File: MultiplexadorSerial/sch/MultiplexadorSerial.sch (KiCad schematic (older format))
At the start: 57 parts, among them Q1 Q_NPN_CBE, Q2 Q_NPN_CBE, Q3 Q_NPN_CBE, Q4 Q_NPN_CBE, U1 SP3481CP, U2 SP3481CP, U3 SP3481CP, U4 SP3481CP, U5 4052

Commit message: Posicionamento MultiplexadorSerial Signed-off-by: cuki2 <mauricio@krebs.com.br>
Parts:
- removed Q1, Q2, Q4: Q_NPN_CBE, symbol Q_NPN_CBE
- added Q1, Q2, Q4: Q_NPN_CBE, w_to:to92_3, symbol Q_NPN_EBC
- D1: footprint w_indicators:led_3mm_red -> w_indicators:led_3mm_green
- Q3: footprint (none) -> w_to:to92_3; symbol Q_NPN_CBE -> Q_NPN_EBC
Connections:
- net GND: now also Q3.1 (E), Q1.1 (E), Q2.1 (E), Q4.1 (E); no longer Q3.3 (E)
- net at R21.2, U3.2 (~RE~), U3.3 (DE): now also Q3.3 (C); no longer Q3.1 (C)
- net at R22.2, U4.2 (~RE~), U4.3 (DE): now also Q4.3 (C)
- net at R18.1: now also Q4.2 (B)
- net at R5.2, U1.2 (~RE~), U1.3 (DE): now also Q1.3 (C)
- net at R1.1: now also Q1.2 (B)
- net at R6.2, U2.2 (~RE~), U2.3 (DE): now also Q2.3 (C)
- net at R2.1: now also Q2.2 (B)
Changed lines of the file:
@@
 $EndComp
 $Comp
-L GND #PWR01
+L GND #PWR21
 U 1 1 59F1E27D
 P 9850 2750
-F 0 "#PWR01" H 9850 2500 50  0001 C CNN
+F 0 "#PWR21" H 9850 2500 50  0001 C CNN
 F 1 "GND" H 9850 2600 50  0000 C CNN
 F 2 "" H 9850 2750 50  0001 C CNN
@@
 $EndComp
 $Comp
-L GND #PWR02
+L GND #PWR13
 U 1 1 59F1F03E
 P 6400 2750
-F 0 "#PWR02" H 6400 2500 50  0001 C CNN
+F 0 "#PWR13" H 6400 2500 50  0001 C CNN
 F 1 "GND" H 6400 2600 50  0000 C CNN
 F 2 "" H 6400 2750 50  0001 C CNN
@@
 $EndComp
 $Comp
-L GND #PWR03
+L GND #PWR11
 U 1 1 59F1FB71
 P 5850 3750
-F 0 "#PWR03" H 5850 3500 50  0001 C CNN
+F 0 "#PWR11" H 5850 3500 50  0001 C CNN
 F 1 "GND" H 5850 3600 50  0000 C CNN
 F 2 "" H 5850 3750 50  0001 C CNN
@@
 $EndComp
 $Comp
-L GND #PWR04
+L GND #PWR15
 U 1 1 59F20200
 P 6450 3900
-F 0 "#PWR04" H 6450 3650 50  0001 C CNN
+F 0 "#PWR15" H 6450 3650 50  0001 C CNN
 F 1 "GND" H 6450 3750 50  0000 C CNN
 F 2 "" H 6450 3900 50  0001 C CNN
@@
 $EndComp
 $Comp
-L GND #PWR05
+L GND #PWR20
 U 1 1 59F215E7
 P 9250 4550
-F 0 "#PWR05" H 9250 4300 50  0001 C CNN
+F 0 "#PWR20" H 9250 4300 50  0001 C CNN
 F 1 "GND" H 9250 4400 50  0000 C CNN
 F 2 "" H 9250 4550 50  0001 C CNN
@@
 $EndComp
 $Comp
-L Q_NPN_CBE Q3
+L Q_NPN_EBC Q3
 U 1 1 59F228FE
 P 4650 3650
 F 0 "Q3" H 4850 3700 50  0000 L CNN
 F 1 "Q_NPN_CBE" H 4850 3600 50  0000 L CNN
-F 2 "" H 4850 3750 50  0001 C CNN
+F 2 "w_to:to92_3" H 4850 3750 50  0001 C CNN
 F 3 "" H 4650 3650 50  0001 C CNN
 	1    4650 3650
@@
 $EndComp
 $Comp
-L GND #PWR06
+L GND #PWR9
 U 1 1 59F22AFE
 P 4750 3950
-F 0 "#PWR06" H 4750 3700 50  0001 C CNN
+F 0 "#PWR9" H 4750 3700 50  0001 C CNN
 F 1 "GND" H 4750 3800 50  0000 C CNN
 F 2 "" H 4750 3950 50  0001 C CNN
@@
 $EndComp
 $Comp
-L GND #PWR07
+L GND #PWR22
 U 1 1 59F26F62
 P 10100 1000
-F 0 "#PWR07" H 10100 750 50  0001 C CNN
+F 0 "#PWR22" H 10100 750 50  0001 C CNN
 F 1 "GND" H 10100 850 50  0000 C CNN
 F 2 "" H 10100 1000 50  0001 C CNN
@@
 $EndComp
 $Comp
-L GND #PWR08
+L GND #PWR18
 U 1 1 59F27359
 P 7650 1700
-F 0 "#PWR08" H 7650 1450 50  0001 C CNN
+F 0 "#PWR18" H 7650 1450 50  0001 C CNN
 F 1 "GND" H 7650 1550 50  0000 C CNN
 F 2 "" H 7650 1700 50  0001 C CNN
@@
 $EndComp
 $Comp
-L GND #PWR09
+L GND #PWR14
 U 1 1 59F28089
 P 6400 5450
-F 0 "#PWR09" H 6400 5200 50  0001 C CNN
+F 0 "#PWR14" H 6400 5200 50  0001 C CNN
 F 1 "GND" H 6400 5300 50  0000 C CNN
 F 2 "" H 6400 5450 50  0001 C CNN
@@
 $EndComp
 $Comp
-L GND #PWR010
+L GND #PWR12
 U 1 1 59F280AE
 P 5850 6450
-F 0 "#PWR010" H 5850 6200 50  0001 C CNN
+F 0 "#PWR12" H 5850 6200 50  0001 C CNN
 F 1 "GND" H 5850 6300 50  0000 C CNN
 F 2 "" H 5850 6450 50  0001 C CNN
@@
 $EndComp
 $Comp
-L GND #PWR011
+L GND #PWR16
 U 1 1 59F280BC
 P 6450 6600
-F 0 "#PWR011" H 6450 6350 50  0001 C CNN
+F 0 "#PWR16" H 6450 6350 50  0001 C CNN
 F 1 "GND" H 6450 6450 50  0000 C CNN
 F 2 "" H 6450 6600 50  0001 C CNN
@@
 $EndComp
 $Comp
-L Q_NPN_CBE Q4
-U 1 1 59F280E2
-P 4650 6350
-F 0 "Q4" H 4850 6400 50  0000 L CNN
-F 1 "Q_NPN_CBE" H 4850 6300 50  0000 L CNN
-F 2 "" H 4850 6450 50  0001 C CNN
-F 3 "" H 4650 6350 50  0001 C CNN
-	1    4650 6350
-	1    0    0    -1
-$EndComp
-$Comp
-L GND #PWR012
+L GND #PWR10
 U 1 1 59F280E9
 P 4750 6650
-F 0 "#PWR012" H 4750 6400 50  0001 C CNN
+F 0 "#PWR10" H 4750 6400 50  0001 C CNN
 F 1 "GND" H 4750 6500 50  0000 C CNN
 F 2 "" H 4750 6650 50  0001 C CNN
@@
 $EndComp
 $Comp
-L GND #PWR013
+L GND #PWR5
 U 1 1 59F2BE74
 P 2850 5650
-F 0 "#PWR013" H 2850 5400 50  0001 C CNN
+F 0 "#PWR5" H 2850 5400 50  0001 C CNN
 F 1 "GND" H 2850 5500 50  0000 C CNN
 F 2 "" H 2850 5650 50  0001 C CNN
@@
 $EndComp
 $Comp
-L GND #PWR014
+L GND #PWR3
 U 1 1 59F2BE99
 P 2300 6650
-F 0 "#PWR014" H 2300 6400 50  0001 C CNN
+F 0 "#PWR3" H 2300 6400 50  0001 C CNN
 F 1 "GND" H 2300 6500 50  0000 C CNN
 F 2 "" H 2300 6650 50  0001 C CNN
@@
 $EndComp
 $Comp
-L GND #PWR015
+L GND #PWR6
 U 1 1 59F2BEA7
 P 2900 6800
-F 0 "#PWR015" H 2900 6550 50  0001 C CNN
+F 0 "#PWR6" H 2900 6550 50  0001 C CNN
 F 1 "GND" H 2900 6650 50  0000 C CNN
 F 2 "" H 2900 6800 50  0001 C CNN
@@
 $EndComp
 $Comp
-L Q_NPN_CBE Q1
-U 1 1 59F2BECC
-P 1100 6550
-F 0 "Q1" H 1300 6600 50  0000 L CNN
-F 1 "Q_NPN_CBE" H 1300 6500 50  0000 L CNN
-F 2 "" H 1300 6650 50  0001 C CNN
-F 3 "" H 1100 6550 50  0001 C CNN
-	1    1100 6550
-	1    0    0    -1
-$EndComp
-$Comp
-L GND #PWR016
+L GND #PWR1
 U 1 1 59F2BED3
 P 1200 6850
-F 0 "#PWR016" H 1200 6600 50  0001 C CNN
+F 0 "#PWR1" H 1200 6600 50  0001 C CNN
 F 1 "GND" H 1200 6700 50  0000 C CNN
 F 2 "" H 1200 6850 50  0001 C CNN
@@
 $EndComp
 $Comp
-L GND #PWR017
+L GND #PWR7
 U 1 1 59F2EBAF
 P 2950 2400
-F 0 "#PWR017" H 2950 2150 50  0001 C CNN
+F 0 "#PWR7" H 2950 2150 50  0001 C CNN
 F 1 "GND" H 2950 2250 50  0000 C CNN
 F 2 "" H 2950 2400 50  0001 C CNN
@@
 $EndComp
 $Comp
-L GND #PWR018
+L GND #PWR4
 U 1 1 59F2EBD4
 P 2400 3400
-F 0 "#PWR018" H 2400 3150 50  0001 C CNN
+F 0 "#PWR4" H 2400 3150 50  0001 C CNN
 F 1 "GND" H 2400 3250 50  0000 C CNN
 F 2 "" H 2400 3400 50  0001 C CNN
@@
 $EndComp
 $Comp
-L GND #PWR019
+L GND #PWR8
 U 1 1 59F2EBE2
 P 3000 3550
-F 0 "#PWR019" H 3000 3300 50  0001 C CNN
+F 0 "#PWR8" H 3000 3300 50  0001 C CNN
 F 1 "GND" H 3000 3400 50  0000 C CNN
 F 2 "" H 3000 3550 50  0001 C CNN
@@
 $EndComp
 $Comp
-L Q_NPN_CBE Q2
-U 1 1 59F2EC07
-P 1200 3300
-F 0 "Q2" H 1400 3350 50  0000 L CNN
-F 1 "Q_NPN_CBE" H 1400 3250 50  0000 L CNN
-F 2 "" H 1400 3400 50  0001 C CNN
-F 3 "" H 1200 3300 50  0001 C CNN
-	1    1200 3300
-	1    0    0    -1
-$EndComp
-$Comp
-L GND #PWR020
+L GND #PWR2
 U 1 1 59F2EC0E
 P 1300 3600
-F 0 "#PWR020" H 1300 3350 50  0001 C CNN
+F 0 "#PWR2" H 1300 3350 50  0001 C CNN
 F 1 "GND" H 1300 3450 50  0000 C CNN
 F 2 "" H 1300 3600 50  0001 C CNN
@@
 F 0 "D1" H 7050 1250 50  0000 C CNN
 F 1 "PWR" H 7050 1050 50  0000 C CNN
-F 2 "w_indicators:led_3mm_red" H 7050 1150 50  0001 C CNN
+F 2 "w_indicators:led_3mm_green" H 7050 1150 50  0001 C CNN
 F 3 "" H 7050 1150 50  0001 C CNN
 	1    7050 1150
@@
 $EndComp
 $Comp
-L GND #PWR021
+L GND #PWR17
 U 1 1 59F4549D
 P 6550 1050
-F 0 "#PWR021" H 6550 800 50  0001 C CNN
+F 0 "#PWR17" H 6550 800 50  0001 C CNN
 F 1 "GND" H 6550 900 50  0000 C CNN
 F 2 "" H 6550 1050 50  0001 C CNN
@@
 	6550 900  6600 900
 $Comp
-L GND #PWR022
+L GND #PWR19
 U 1 1 59F4914C
 P 7950 4250
-F 0 "#PWR022" H 7950 4000 50  0001 C CNN
+F 0 "#PWR19" H 7950 4000 50  0001 C CNN
 F 1 "GND" H 7950 4100 50  0000 C CNN
 F 2 "" H 7950 4250 50  0001 C CNN
@@
 Wire Wire Line
 	7950 3850 8100 3850
+$Comp
+L Q_NPN_EBC Q4
+U 1 1 59F58E6E
+P 4650 6350
+F 0 "Q4" H 4850 6400 50  0000 L CNN
+F 1 "Q_NPN_CBE" H 4850 6300 50  0000 L CNN
+F 2 "w_to:to92_3" H 4850 6450 50  0001 C CNN
+F 3 "" H 4650 6350 50  0001 C CNN
+	1    4650 6350
+	1    0    0    -1
+$EndComp
+$Comp
+L Q_NPN_EBC Q1
+U 1 1 59F58F65
+P 1100 6550
+F 0 "Q1" H 1300 6600 50  0000 L CNN
+F 1 "Q_NPN_CBE" H 1300 6500 50  0000 L CNN
+F 2 "w_to:to92_3" H 1300 6650 50  0001 C CNN
+F 3 "" H 1100 6550 50  0001 C CNN
+	1    1100 6550
+	1    0    0    -1
+$EndComp
+$Comp
+L Q_NPN_EBC Q2
+U 1 1 59F59073
+P 1200 3300
+F 0 "Q2" H 1400 3350 50  0000 L CNN
+F 1 "Q_NPN_CBE" H 1400 3250 50  0000 L CNN
+F 2 "w_to:to92_3" H 1400 3400 50  0001 C CNN
+F 3 "" H 1200 3300 50  0001 C CNN
+	1    1200 3300
+	1    0    0    -1
+$EndComp
 $EndSCHEMATC

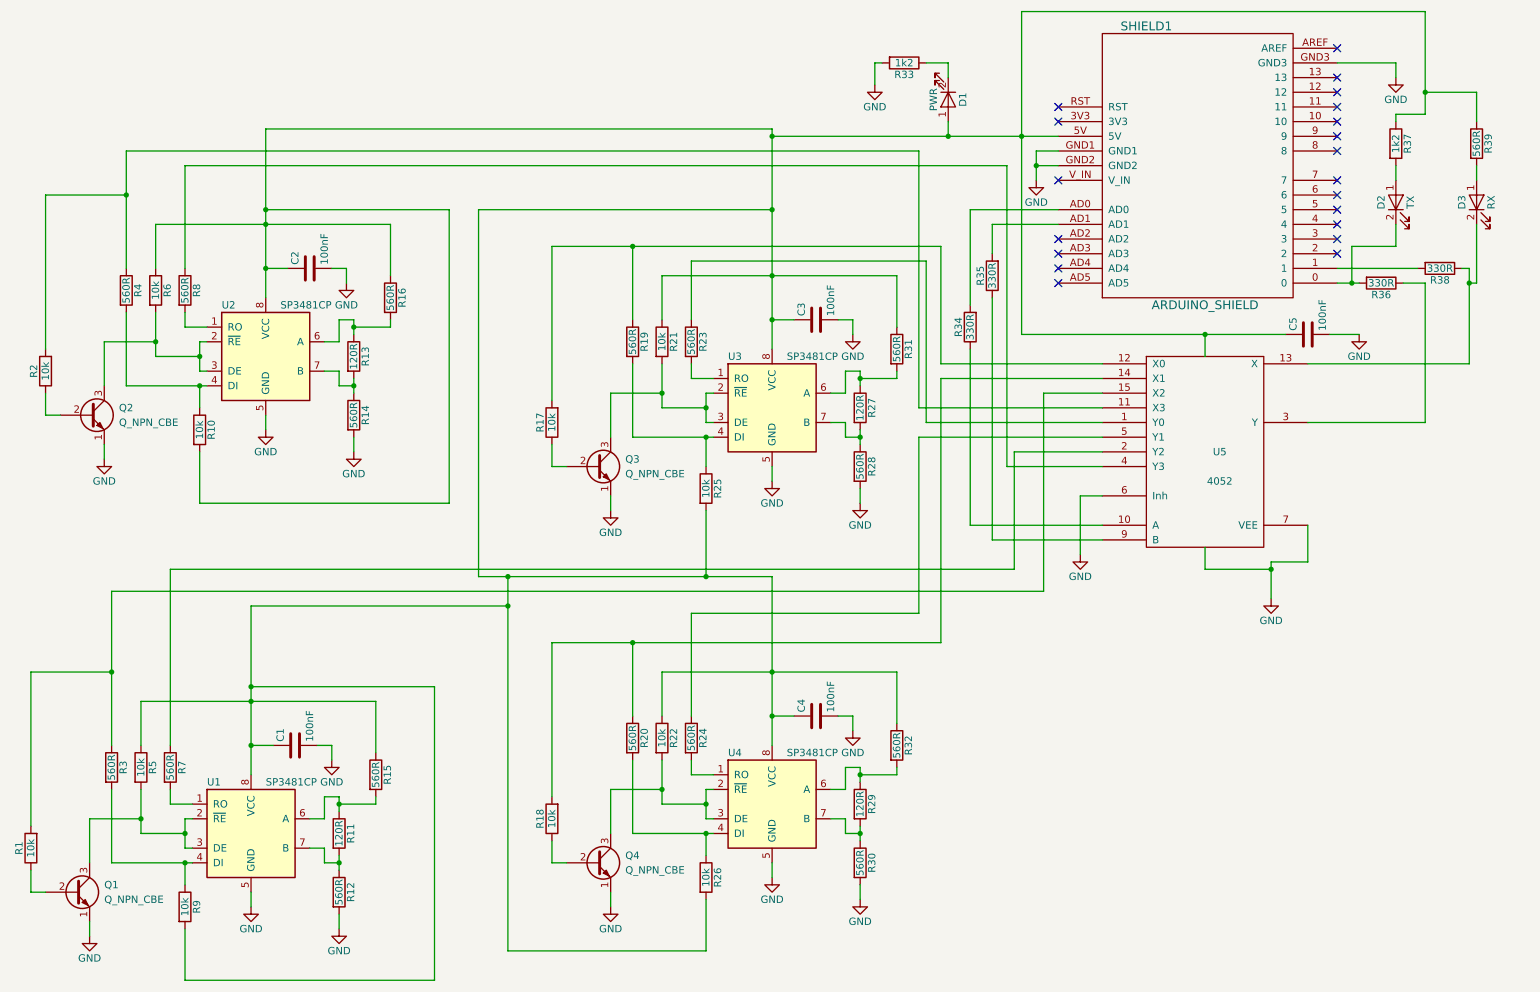
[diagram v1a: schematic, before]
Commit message: Multiplexador Serial RS485 arduino
Signed-off-by: cuki2 <mauricio@krebs.com.br>
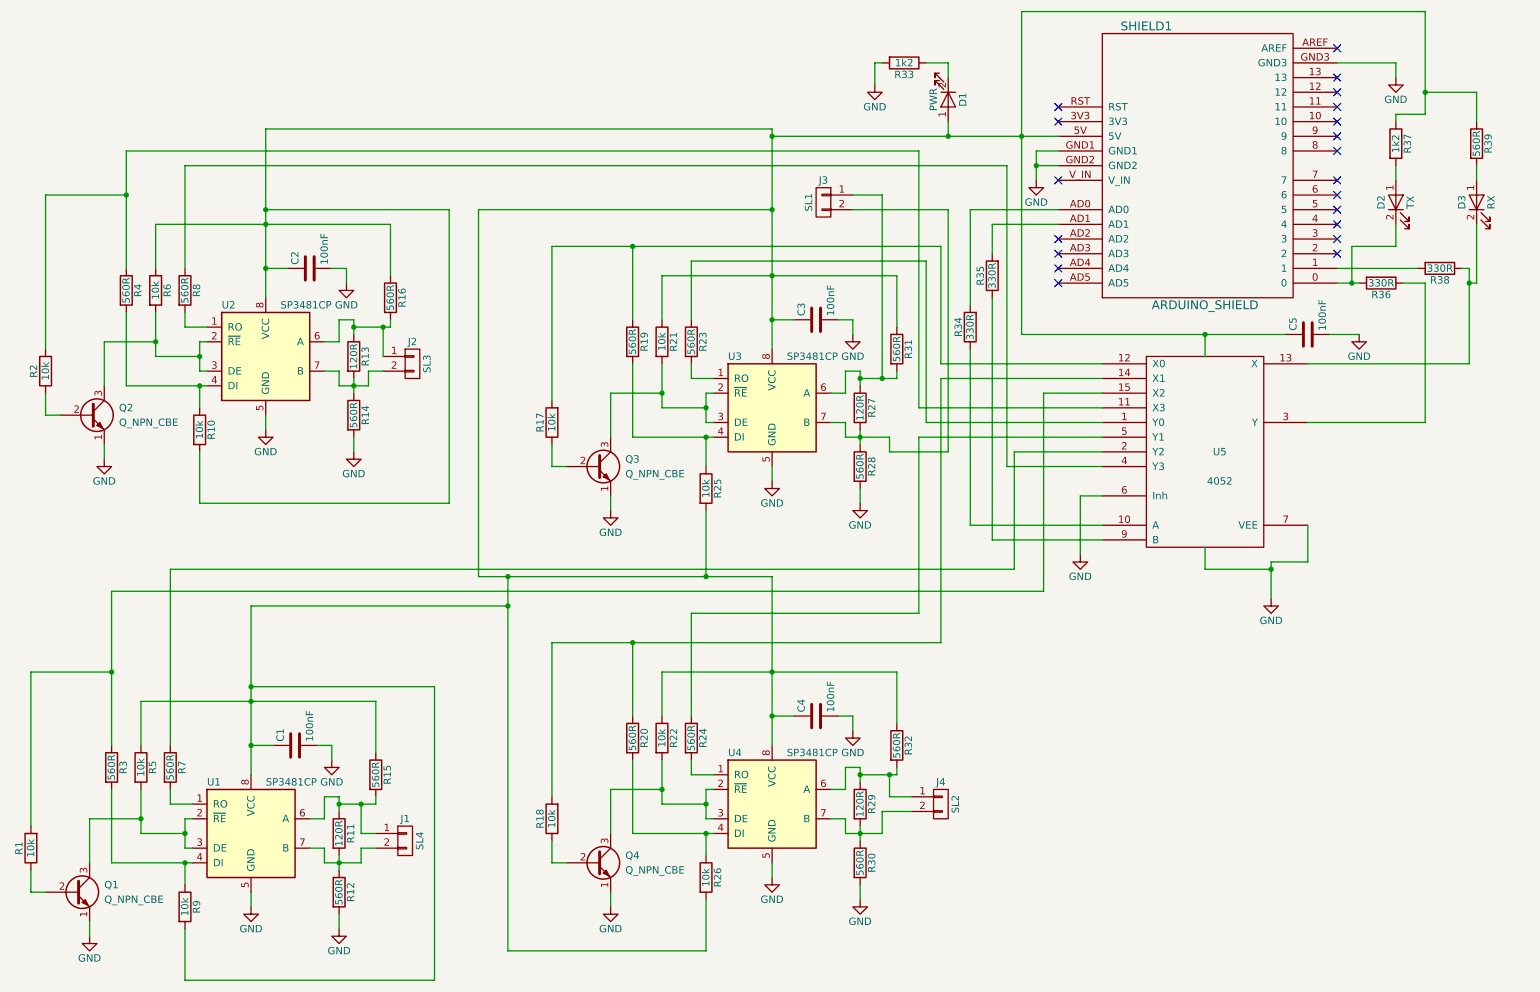
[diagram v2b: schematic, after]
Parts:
- added J1: SL4, w_pin_strip:pin_socket_2, symbol CONN_01X02
- added J2: SL3, w_pin_strip:pin_socket_2, symbol CONN_01X02
- added J3: SL1, w_pin_strip:pin_socket_2, symbol CONN_01X02
- added J4: SL2, w_pin_strip:pin_socket_2, symbol CONN_01X02
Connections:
- net at R27.1, R31.2, U3.6 (A): now also J3.1 (P1)
- net at R27.2, R28.1, U3.7 (B): now also J3.2 (P2)
- net at R29.1, R32.2, U4.6 (A): now also J4.1 (P1)
- net at R29.2, R30.1, U4.7 (B): now also J4.2 (P2)
- net at R11.1, R15.2, U1.6 (A): now also J1.1 (P1)
- net at R11.2, R12.1, U1.7 (B): now also J1.2 (P2)
- net at R13.1, R16.2, U2.6 (A): now also J2.1 (P1)
- net at R13.2, R14.1, U2.7 (B): now also J2.2 (P2)

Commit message: adicionado resistores pull ups nos transdutores
Signed-off-by: cuki2 <mauricio@krebs.com.br>
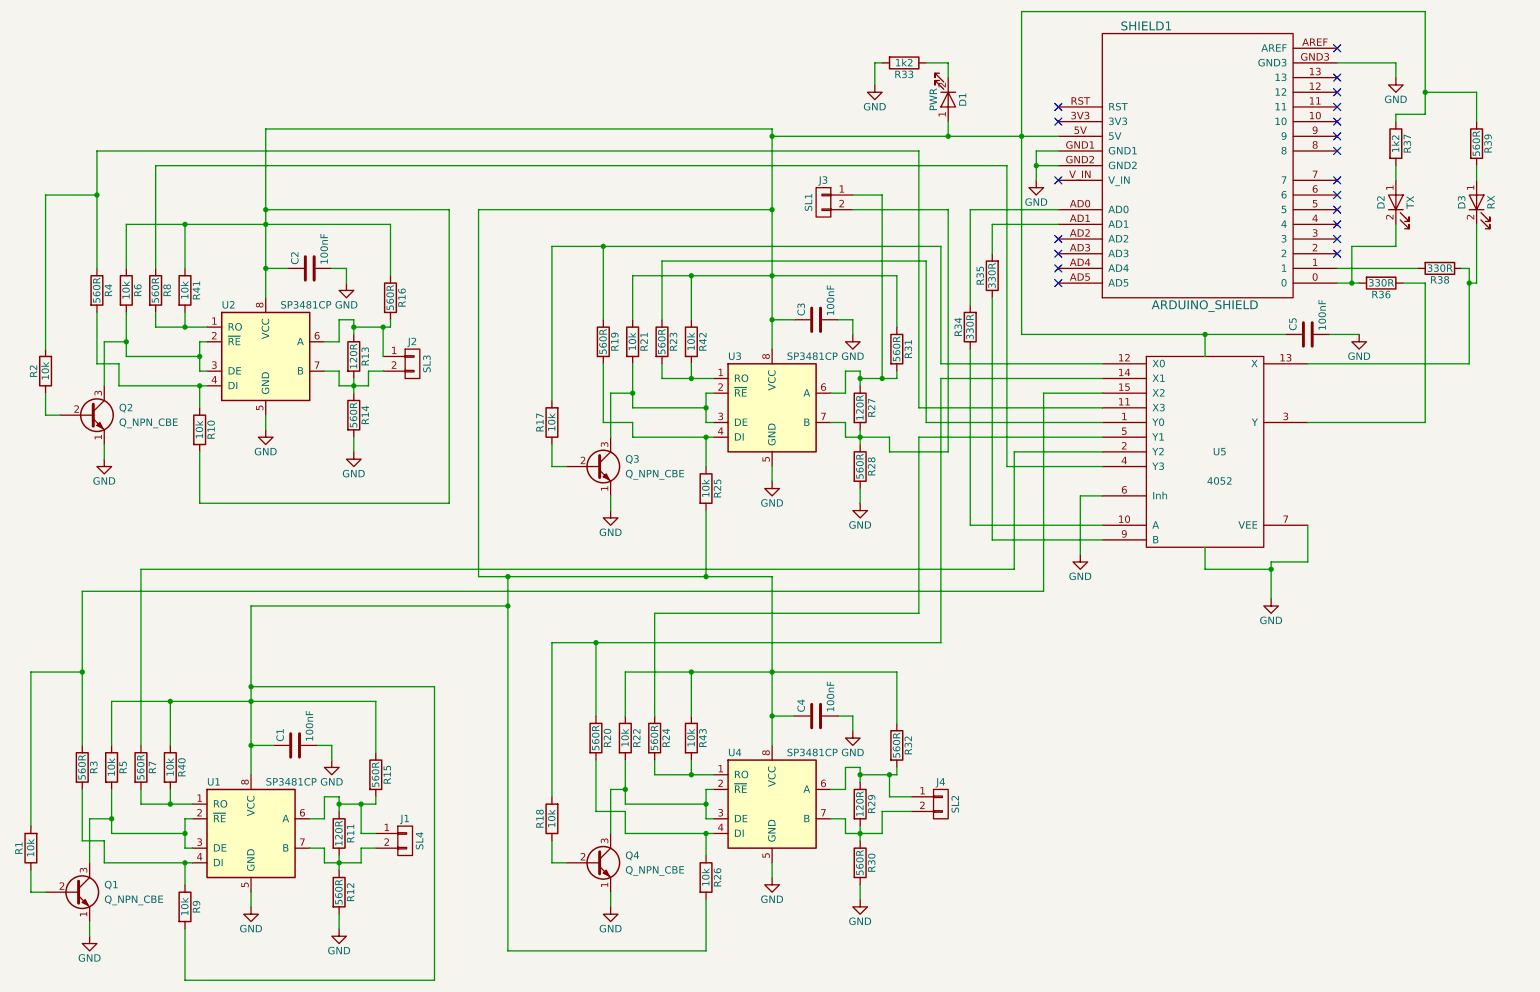
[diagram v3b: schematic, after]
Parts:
- added R40, R41, R42, R43: 10k, w_pth_resistors:rc05_vert, symbol R
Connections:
- net VDD: now also R40.1, R41.1, R42.1, R43.1
- net at R23.2, U3.1 (RO): now also R42.2
- net at R24.2, U4.1 (RO): now also R43.2
- net at R7.2, U1.1 (RO): now also R40.2
- net at R8.2, U2.1 (RO): now also R41.2
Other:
- moved on the sheet: R19, R20, R21, R22, R23, R24, R3, R4, R5, R6, R7, R8

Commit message: placa em smd
Signed-off-by: cuki2 <mauricio@krebs.com.br>
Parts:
- C1, C2, C3, C4, C5: footprint w_capacitors:cnp_6mm_disc -> w_smd_cap:c_0805
- D1: footprint w_indicators:led_3mm_green -> w_smd_leds:Led_0805
- D2: footprint w_indicators:led_3mm_red -> w_smd_leds:Led_0805
- D3: footprint w_indicators:led_3mm_clear -> w_smd_leds:Led_0805
- Q1, Q2, Q3, Q4: footprint w_to:to92_3 -> w_smd_trans:sot23
- R1, R10, R11, R12, R13, R14, R15, R16, R17, R18, R19, R2, R20, R21, R22, R23, R24, R25, R26, R27, R28, R29, R3, R30, R31, R32, R33, R34, R35, R36, R37, R38, R39, R4, R40, R41, R42, R43, R5, R6, R7, R8, R9: footprint w_pth_resistors:rc05_vert -> w_smd_resistors:r_0805
- U1, U2, U3, U4: footprint w_pth_circuits:dil_8-300_socket -> w_smd_dil:so-8
- U5: footprint w_pth_circuits:dil_16-300_socket -> w_smd_dil:so-16

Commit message: novo desenho
Signed-off-by: cuki2 <mauricio@krebs.com.br>
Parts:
- removed C1, C2, C3, C4, C5: 100nF, w_smd_cap:c_0805, symbol C
- removed D3: RX, w_smd_leds:Led_0805, symbol M_LED
- removed J1: SL4, w_pin_strip:pin_socket_2, symbol CONN_01X02
- removed J2: SL3, w_pin_strip:pin_socket_2, symbol CONN_01X02
- removed J4: SL2, w_pin_strip:pin_socket_2, symbol CONN_01X02
- removed Q1, Q2, Q3, Q4: Q_NPN_CBE, w_smd_trans:sot23, symbol Q_NPN_EBC
- removed R1, R10, R17, R18, R2, R21, R22, R25, R26, R40, R41, R42, R43, R5, R6, R9: 10k, w_smd_resistors:r_0805, symbol R
- removed R11, R13, R27, R29: 120R, w_smd_resistors:r_0805, symbol R
- removed R12, R14, R15, R16, R19, R20, R23, R24, R28, R3, R30, R31, R32, R39, R4, R7, R8: 560R, w_smd_resistors:r_0805, symbol R
- removed R34, R35, R36, R38: 330R, w_smd_resistors:r_0805, symbol R
- removed U1, U2, U3, U4: SP3481CP, w_smd_dil:so-8, symbol SP3481CP
- removed U5: 4052, w_smd_dil:so-16, symbol 4052
- J1: renamed from J3; value SL1 -> SL; footprint w_pin_strip:pin_socket_2 -> w_pin_strip:pin_socket_3; symbol CONN_01X02 -> CONN_01X03
- renumbered D2 to D1, D1 to D2, R37 to R1, R33 to R2
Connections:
- net GND: now also J1.3 (P3), R2.1; no longer R2.2
- net RX: now reaches SHIELD1.0
- net RX: now also J1.2 (P2); no longer D1.2 (K)
- net TX: now reaches SHIELD1.1
- net TX: now also D1.2 (K), J1.1 (P1)
- net ADR0: now reaches SHIELD1.AD0
- net ADR1: now reaches SHIELD1.AD1
- net at D2.2 (K): now also R2.2; no longer R2.1
- net VDD renamed +5V
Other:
- moved on the sheet: D1, D2, R1, R2, SHIELD1
